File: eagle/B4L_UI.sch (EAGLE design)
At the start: 44 parts

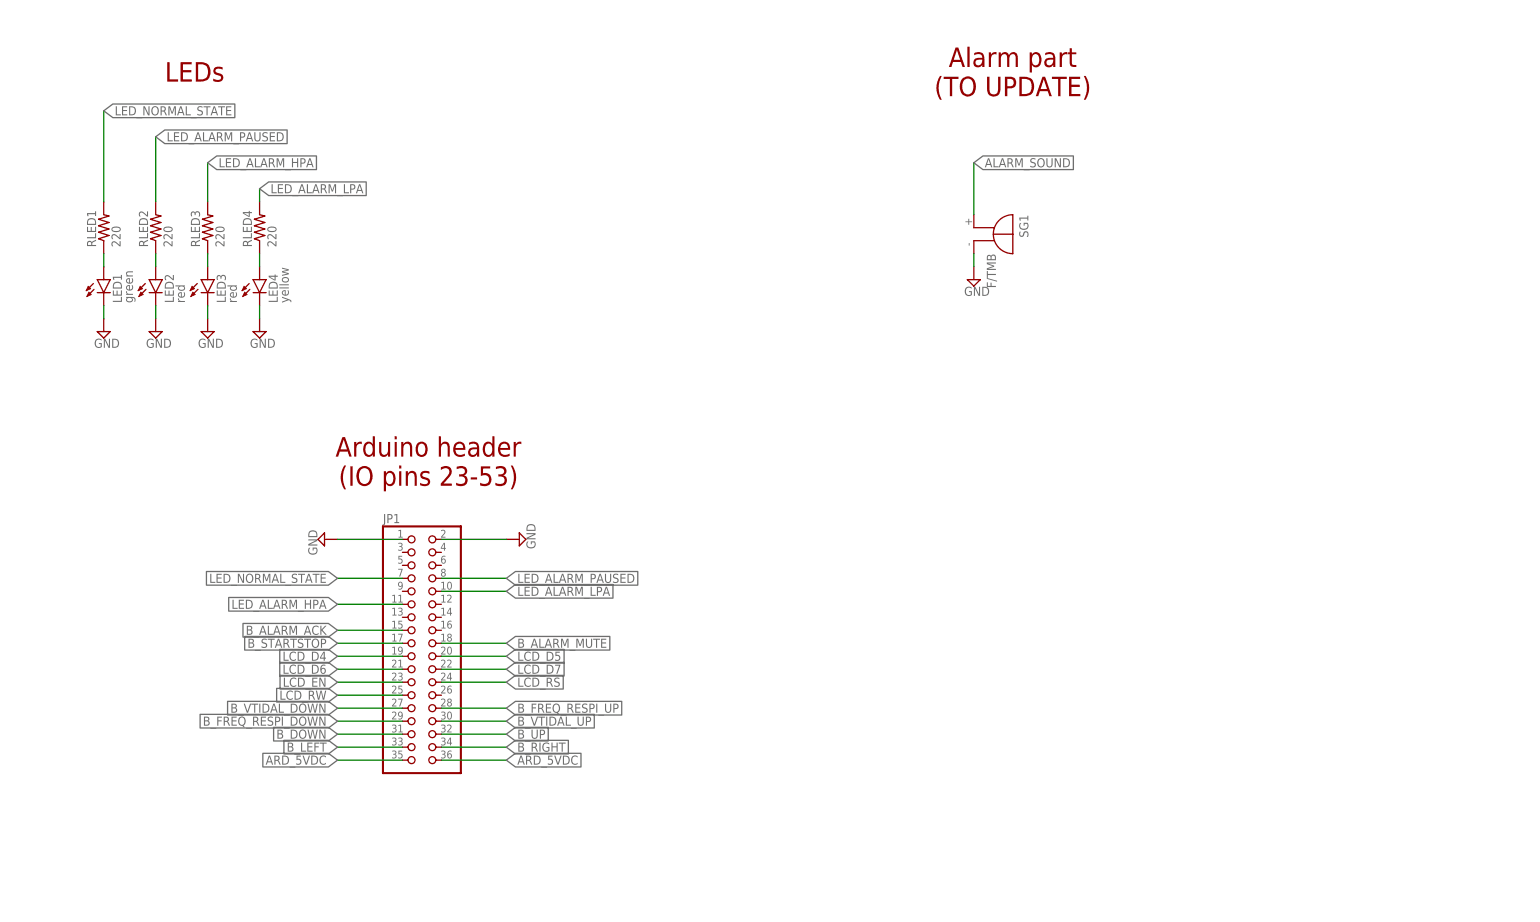
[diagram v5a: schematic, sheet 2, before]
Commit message: [UI board] Update of buzzer driving circuit
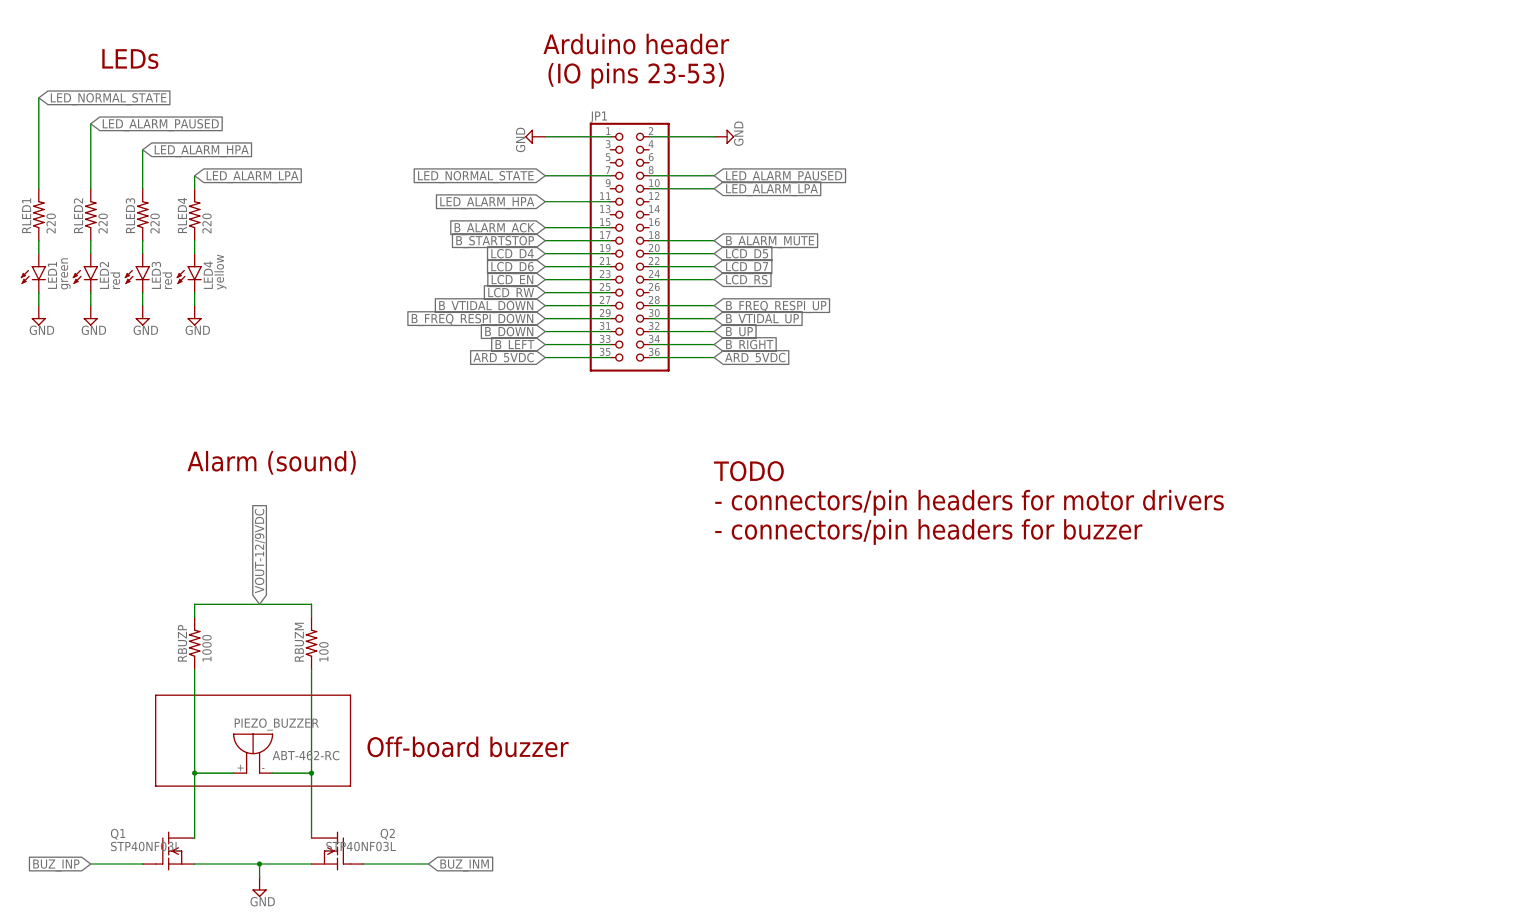
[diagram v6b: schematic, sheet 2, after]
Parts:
- removed SG1: F/TMB, buzzer:F/TMB
- added PIEZO_BUZZER: ABT-462-RC, buzzer:F/TMB
- added Q1, Q2: STP40NF03L, transistor-fet:BUZ10
- added RBUZM: 100, rcl:R-US_0309/12
- added RBUZP: 1000, rcl:R-US_0309/12
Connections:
- removed net ALARM_SOUND: SG1.+
- new net BUZ_INM: Q2.G
- new net BUZ_INP: Q1.G
- new net N$12: PIEZO_BUZZER.+, Q1.D, RBUZP.1
- new net N$14: PIEZO_BUZZER.-, Q2.D, RBUZM.1
- new net VOUT-12/9VDC: RBUZM.2, RBUZP.2
- net GND: now also Q1.S, Q2.S; no longer SG1.-
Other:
- note added: "Alarm (sound)"
- note added: "Off-board buzzer"
- note added: "TODO - connectors/pin headers for motor drivers - connectors/pin headers for buzzer"
- note removed: "Alarm part (TO UPDATE)"
- moved on the sheet: JP1, LED1, LED2, LED3, LED4, RLED1, RLED2, RLED3, RLED4

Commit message: Add motor, lim switch & flow sensor connexions to UI board
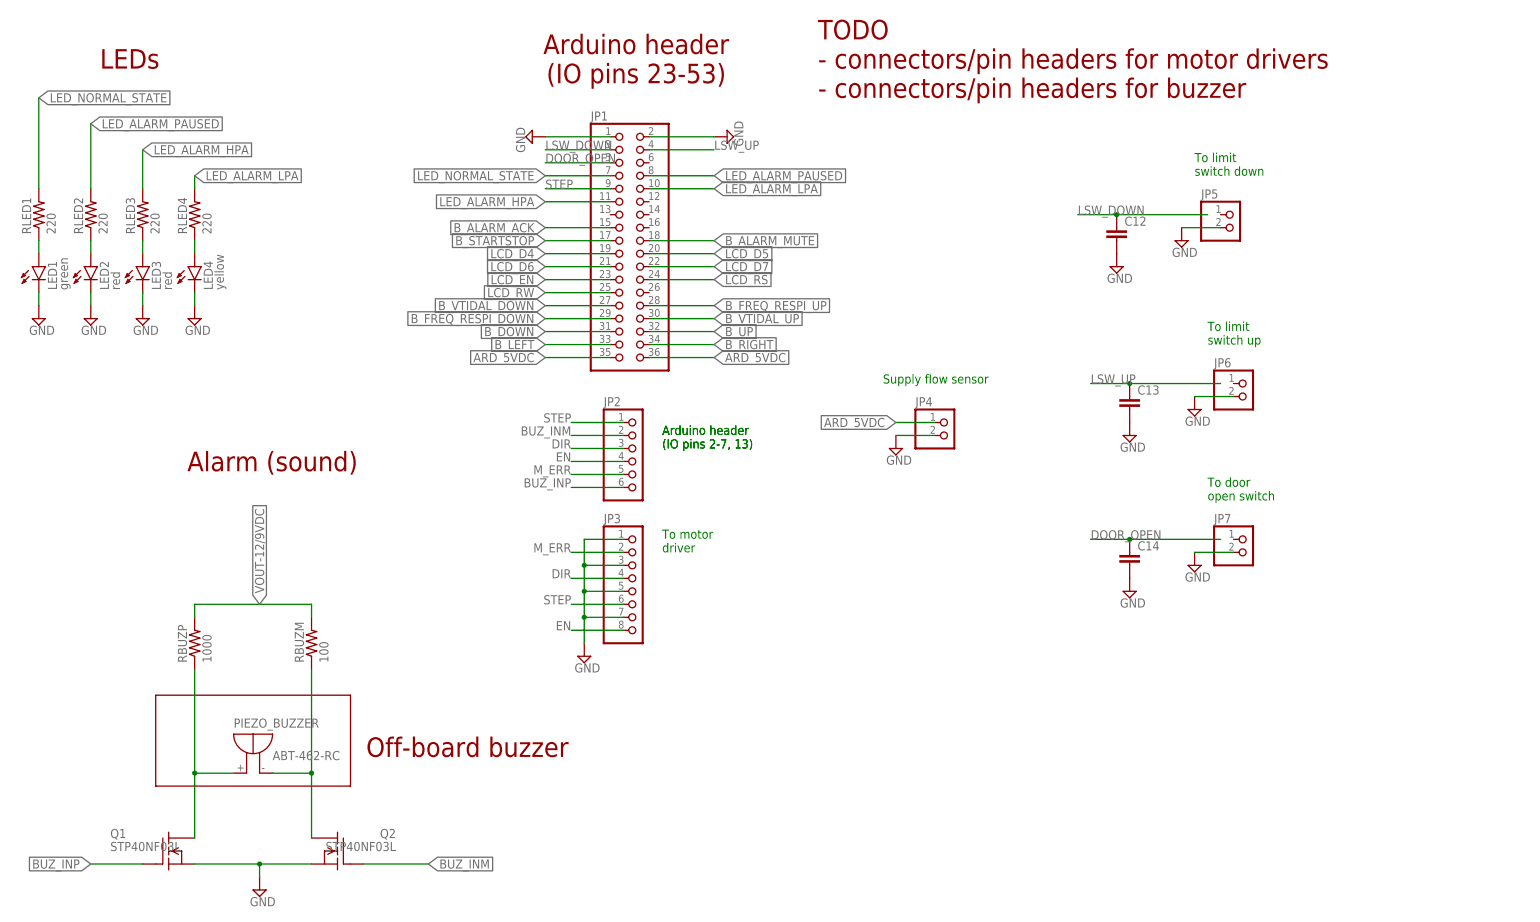
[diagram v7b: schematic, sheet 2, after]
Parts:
- added C12, C13, C14: (no value), capacitor-wima:C2,5-3
- added JP2: (no value), pinhead:PINHD-1X6
- added JP3: (no value), pinhead:PINHD-1X8
- added JP4, JP5, JP6, JP7: (no value), pinhead:PINHD-1X2
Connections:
- new net ARD5VDC: JP4.1
- new net DIR: JP2.3, JP3.4
- new net DOOR_OPEN: C14.1, JP1.5
- new net EN: JP2.4, JP3.8
- new net LSW_DOWN: C12.1, JP1.3
- new net LSW_UP: C13.1, JP1.4
- new net M_ERR: JP2.5, JP3.2
- new net STEP: JP1.9, JP2.1, JP3.6
- net BUZ_INM: now also JP2.2
- net BUZ_INP: now also JP2.6
- net GND: now also C12.2, C13.2, C14.2, JP3.1, JP3.3, JP3.5, JP3.7, JP4.2, JP5.2, JP6.2, JP7.2
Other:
- note added: "Arduino header (IO pins 2-7, 13)"
- note added: "Supply flow sensor"
- note added: "To door open switch"
- note added: "To limit switch down"
- note added: "To limit switch up"
- note added: "To motor driver"

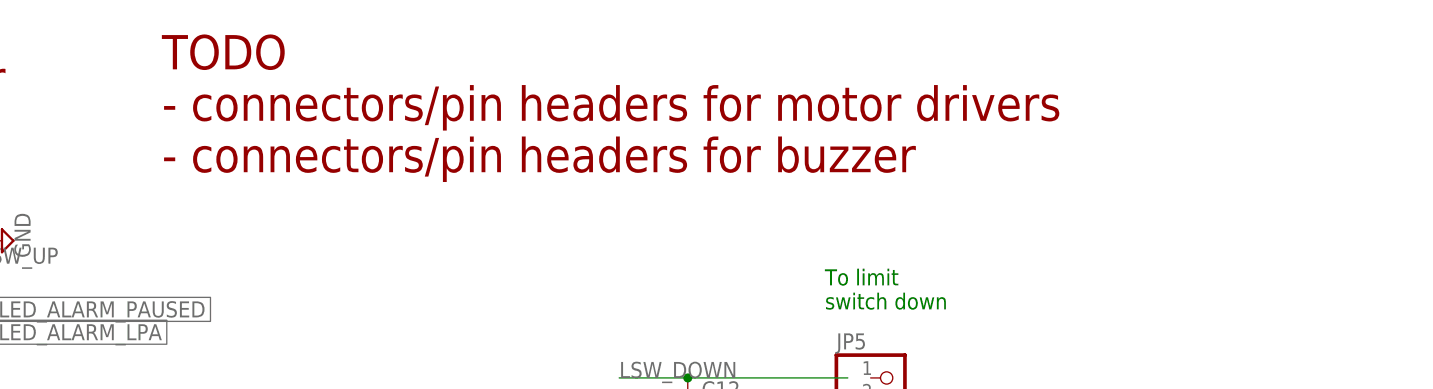
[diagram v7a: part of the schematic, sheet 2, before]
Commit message: update TODO
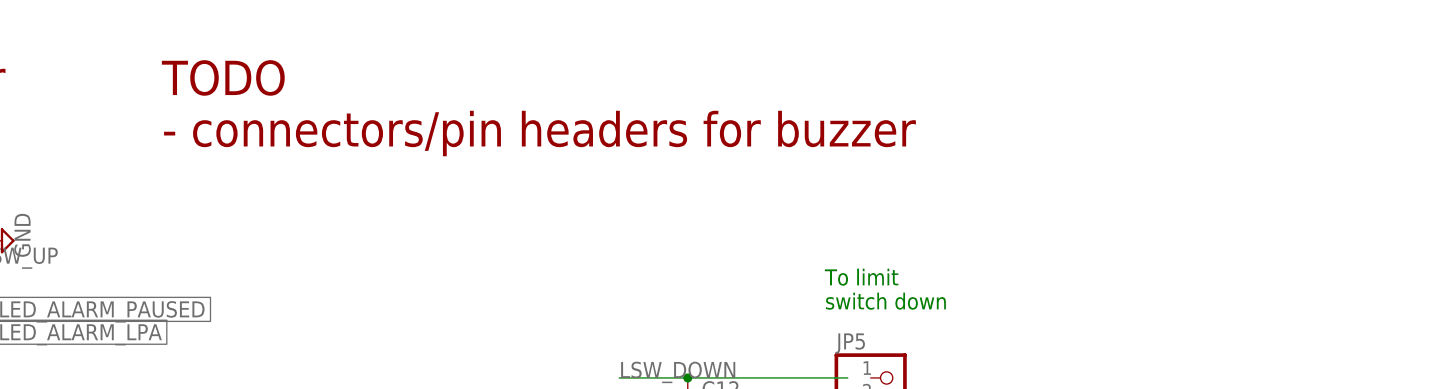
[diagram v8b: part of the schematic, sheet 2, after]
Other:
- note added: "TODO - connectors/pin headers for buzzer"
- note removed: "TODO - connectors/pin headers for motor drivers - connectors/pin headers for buzzer"
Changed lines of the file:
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@@
 <wire x1="33.02" y1="27.94" x2="33.02" y2="45.72" width="0.1524" layer="94"/>
 <text x="162.56" y="170.18" size="3.81" layer="94" align="center-left">TODO
-- connectors/pin headers for motor drivers
 - connectors/pin headers for buzzer</text>
 <text x="132.08" y="93.98" size="1.778" layer="91">Arduino header
